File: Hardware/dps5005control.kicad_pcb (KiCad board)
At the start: 2 copper layers, 50 x 60.5 mm, 24 parts, among them J1 CONN_01X07, P1 5mm_screw_term, P3 ISP, P4 CONN_7, U1 LM7805CT, U2 ATTINY2313-20PU

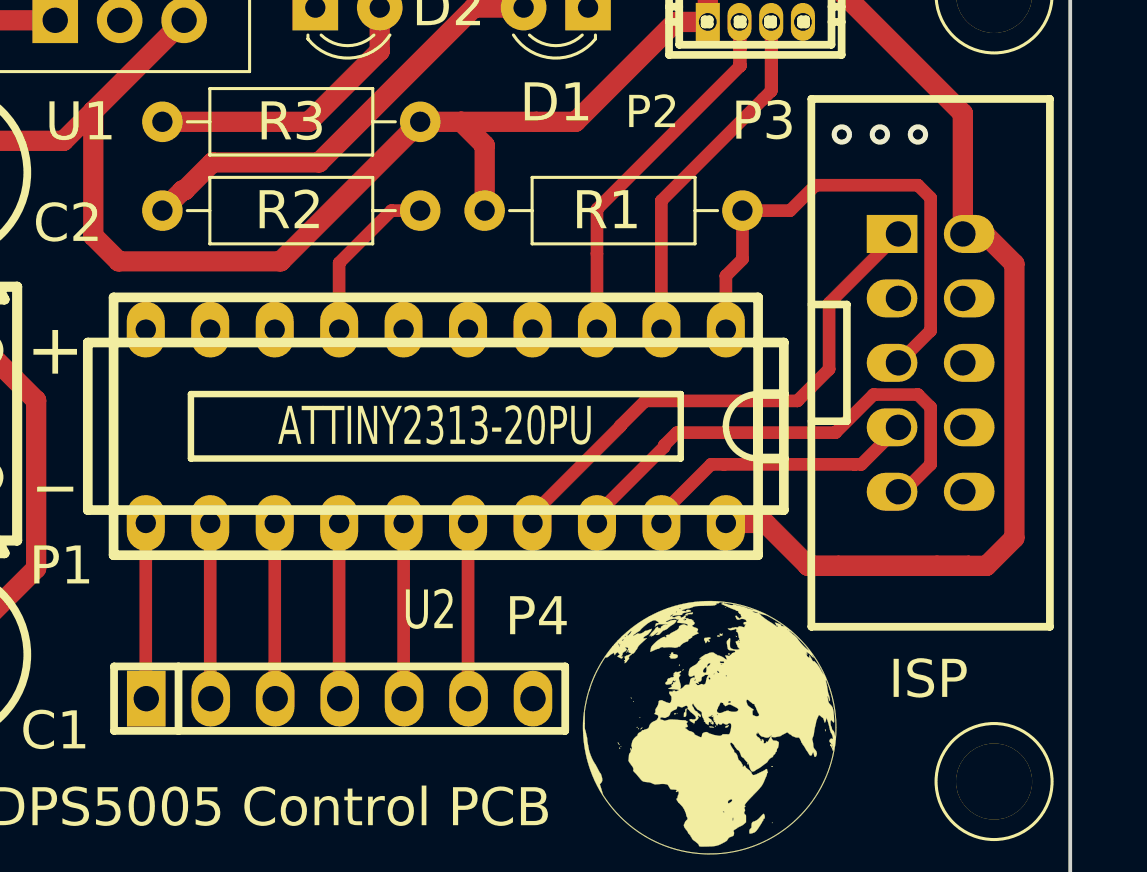
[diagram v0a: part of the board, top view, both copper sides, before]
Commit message: Changed 5 volts to 3.3 volts.
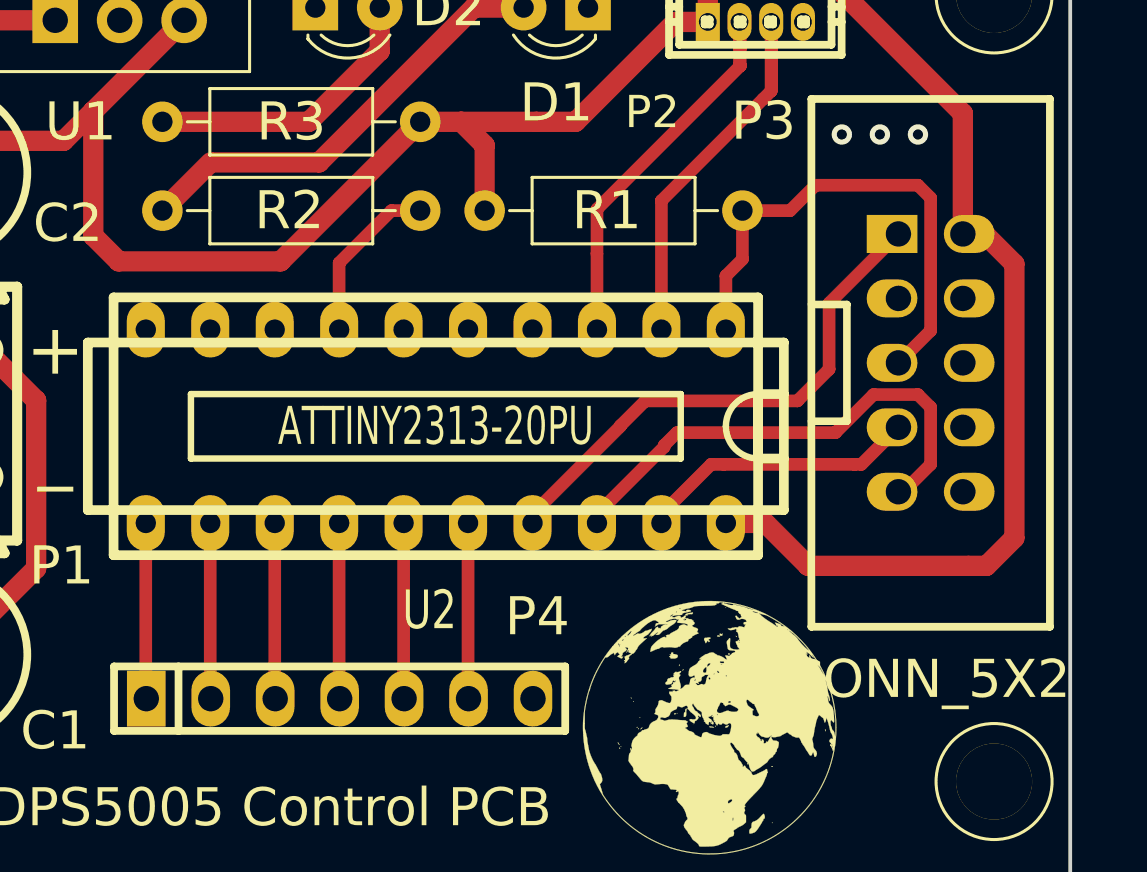
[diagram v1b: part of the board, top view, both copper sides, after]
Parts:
- P1: value 5mm_screw_term -> CONN_2
- P3: value ISP -> CONN_5X2
- U1: value LM7805CT -> LM77833
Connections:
- net /+5v renamed /+3.3v
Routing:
- net /+3.3v: track 100.0 -> 93.7 mm

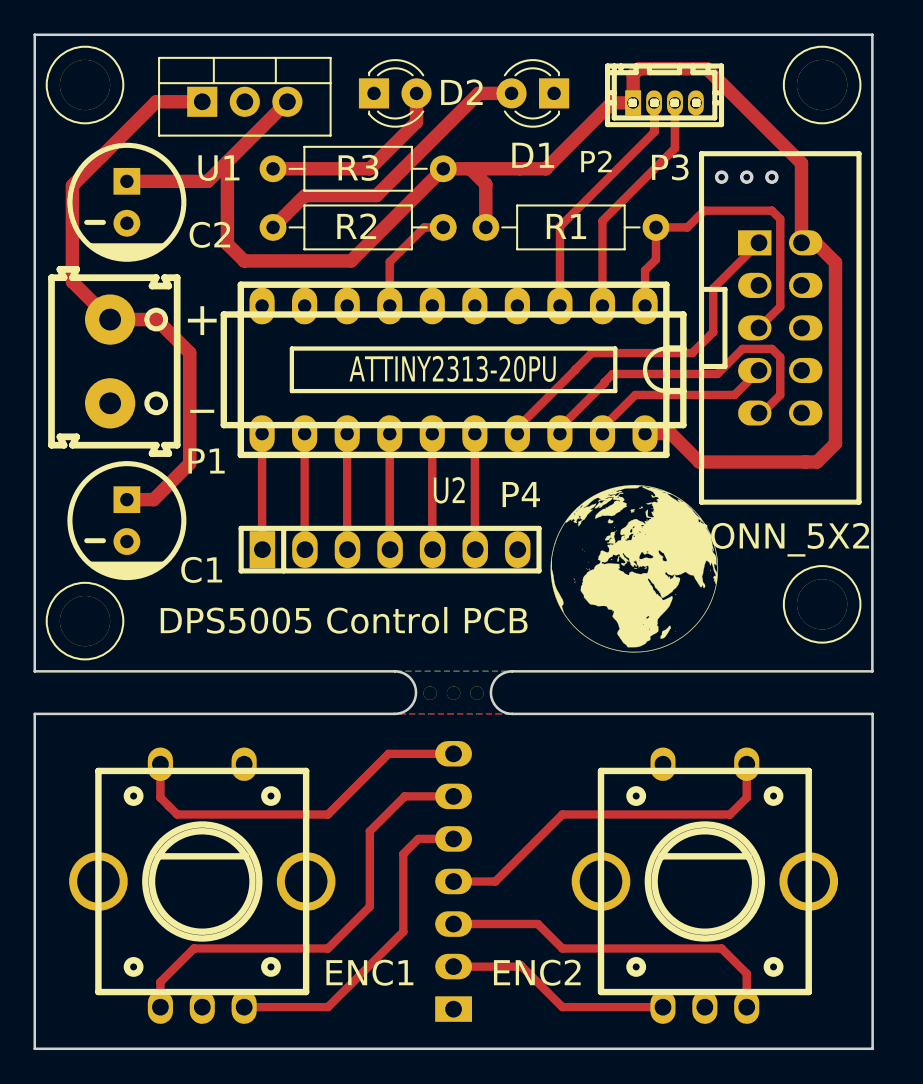
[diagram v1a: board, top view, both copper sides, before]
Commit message: Rotated P2. Added Open Hardware Logo. Cosmetic changes.
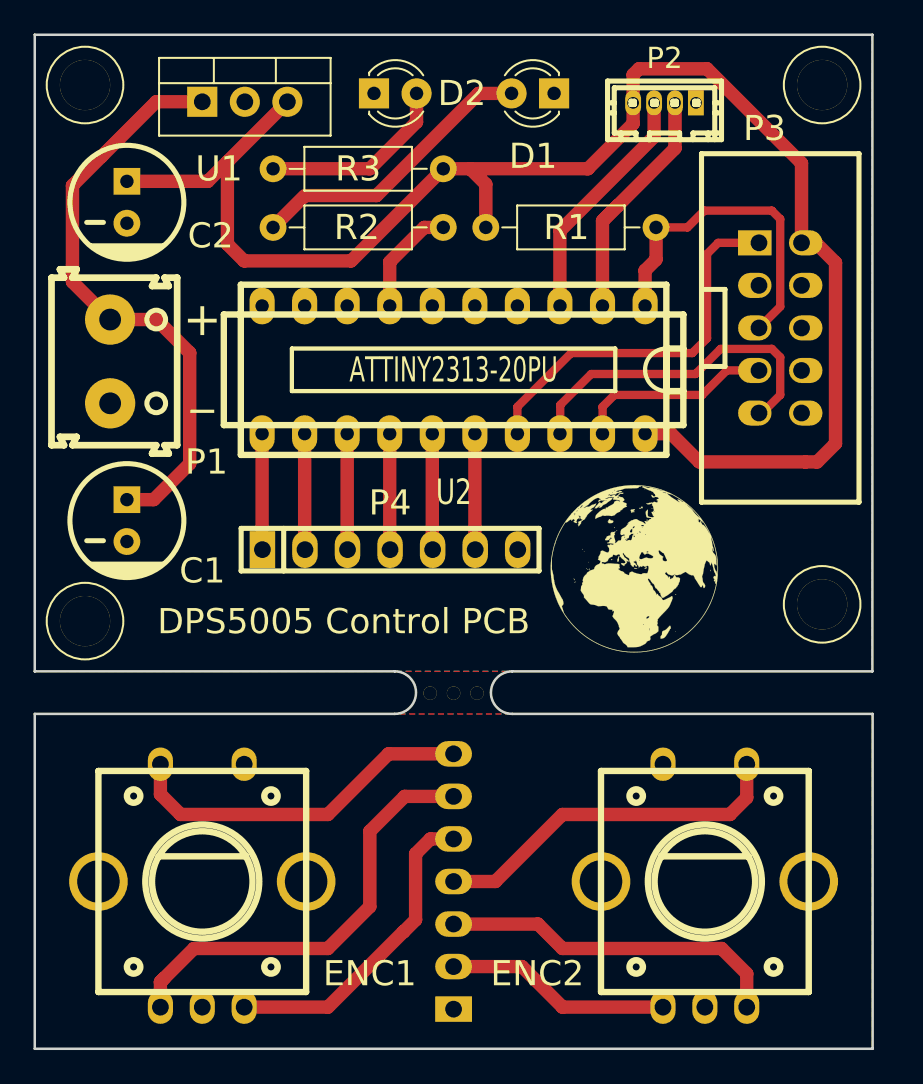
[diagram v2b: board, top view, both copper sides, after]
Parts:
- added G***: LOGO, dps5005-control_board:OpenHardwareLogo, B.Cu at (192.4, 107.6)
- added G***: LOGO, dps5005-control_board:OpenHardwareLogo, B.Cu at (171.7, 66.7)
- turned df13-4p-125dsa to 0 degrees
- renumbered J1 to P1
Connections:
- df13-4p-125dsa pad 1: /+3.3v -> GND
- df13-4p-125dsa pad 2: /Tx -> /Rx
- df13-4p-125dsa pad 3: /Rx -> /Tx
- df13-4p-125dsa pad 4: GND -> /+3.3v
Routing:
- net /_ENC1_A: track 26.2 -> 29.1 mm
- net /MOSI: track 20.9 -> 23.0 mm
- net /Tx: track 16.4 -> 14.5 mm
- net /Rx: track 16.1 -> 17.4 mm
- net /MISO: track 19.7 -> 20.4 mm
- net /SCK: track 11.1 -> 11.8 mm
- net /+3.3v: track 93.7 -> 94.4 mm
- net GND: vias 3 -> 0
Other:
- board text added: "3.3"
- board text added: "CC"
- board text added: "GND"
- board text added: "LED"
- board text added: "Rx"
- board text added: "Tx"
